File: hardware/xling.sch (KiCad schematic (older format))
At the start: 54 parts, among them J4 USB_OTG, J5 AVR ISP, J6 Battery, Q1 NTR0202PL, Q2 NTR0202PL, Q3 NTA4153N, SW2 BTN, SW3 BTN, SW4 BTN, U1 LT1109CZ-12, U2 ATMEGA328P-AU, U3 DEP_128064I, U4 MCP73831, U5 AP3401_TSOT26, Y1 8MHz

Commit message: patch 0.2.5: New OLED.
There is a huge change in a circuit to replace an OLED and fix multiple
mistakes and improve it a bit.
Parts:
- removed C10: 33uF, Xling Footprints:CP_EIA-6032-20_AVX-F, symbol xling:CP
- removed D3: 1N5818, Xling Footprints:D_DO-41_SOD81_P7.62mm_Horizontal, symbol xling:1N5818
- removed L2: 22uH, Xling Footprints:L_7.3x7.3_H3.5, symbol xling:L_Core_Ferrite
- removed Q2: NTR0202PL, Xling Footprints:SOT-23, symbol xling:NTR2101P
- removed Q3: NTA4153N, Xling Footprints:SC-75_SOT-416, symbol xling:NTA4153N
- removed R1, R10: 100K, Xling Footprints:R_1206_3216Metric, symbol xling:R
- removed R11: 191K, Xling Footprints:R_0805_2012Metric, symbol xling:R
- removed R16: 27K, Xling Footprints:R_0603_1608Metric, symbol xling:R
- removed R2: 910K, Xling Footprints:R_1206_3216Metric, symbol xling:R
- removed U1: LT1109CZ-12, Xling Footprints:TO-92_LT1109CZ, symbol xling:LT1109CZ-12
- removed U3: DEP_128064I, Xling Footprints:XF2M_24151AR100_SMD_1x24_Pitch_0.5mm, symbol xling:DEP_128064I
- added C10: 0.22uF, Xling Footprints:C_0603_1608Metric, symbol xling:C
- added C12, C2, C3, C4: 4.7uF, symbol xling:C
- added C7: 100nF, symbol xling:C
- added L1: 10uH, symbol xling:L
- added R3: 10K, symbol xling:R
- added R6, R7: 510K, Xling Footprints:R_0603_1608Metric, symbol xling:R
- added U1: REX012864L, Xling Footprints:DisplayPin_1x30_P0.7mm, symbol xling:REX012864L
- C1: renamed from C7; footprint Xling Footprints:C_0805_2012Metric -> (none); Model CC0805KRX7R9BB472 -> (none)
- C11: value 2.2uF -> 0.22uF; Model 0603ZD225KAT2A -> (none)
- C13: renamed from C20; footprint Xling Footprints:C_0805_2012Metric -> (none); Model CC0805KRX7R9BB472 -> (none)
- C14: renamed from C19; footprint Xling Footprints:C_0805_2012Metric -> (none); Model CC0805KRX7R9BB472 -> (none)
- C15: renamed from C18; footprint Xling Footprints:C_0805_2012Metric -> (none); Model CC0805KRX7R9BB472 -> (none)
- C16: renamed from C1; footprint Xling Footprints:C_0805_2012Metric -> (none); Model CL21C220JBANNNC -> (none)
- C17: renamed from C6; footprint Xling Footprints:C_1206_3216Metric -> (none); Model CL31B475KAHNNNE -> (none)
- C18: renamed from C2; footprint Xling Footprints:C_1206_3216Metric -> (none); Model CL31B475KAHNNNE -> (none)
- C19: renamed from C5; footprint Xling Footprints:C_1206_3216Metric -> (none); Model CL31B475KAHNNNE -> (none)
- C20: renamed from C3; footprint Xling Footprints:C_1206_3216Metric -> (none); Model CL31B475KAHNNNE -> (none)
- C5: renamed from C15; footprint Xling Footprints:C_0805_2012Metric -> (none); Model CL21C220JBANNNC -> (none)
- C6: renamed from C8; footprint Xling Footprints:C_0805_2012Metric -> (none); Model CL21B104JBCNNNC -> (none)
- C8: renamed from C13; footprint Xling Footprints:C_0805_2012Metric -> (none); Model CL21C220JBANNNC -> (none)
- C9: value 1pF -> 100nF; footprint Xling Footprints:C_0805_2012Metric -> (none); Model CL21C010BBANNNC -> (none)
- D1: renamed from D5; value 1N5818 -> 1N5819; footprint Xling Footprints:D_DO-41_SOD81_P7.62mm_Horizontal -> (none); Model 1N5819 -> 1N5819HW-7-F
- J1: renamed from J5; value AVR ISP -> ISP; footprint Xling Footprints:IDC-Header_2x03_P2.54mm_Vertical -> (none); Model T821106A1S100CEU -> (none)
- J2: renamed from J4; footprint Xling Footprints:USB_Mini-B_Lumberg_2486_01_Horizontal -> (none); Model Molex 67503-1020 -> 105017-0001
- J3: renamed from J6; footprint Xling Footprints:PinHeader_1x02_P2.54mm_Horizontal -> (none); Model DS1022-1*20RDF1-1 -> (none)
- L2: renamed from L1; footprint Xling Footprints:L_1210_3225Metric -> (none); Model NLV10JT2R2 -> NLV32T-2R2J-PF
- R10: renamed from R17; footprint Xling Footprints:R_1206_3216Metric -> (none); Model CRCW1206100KFKTABC -> (none)
- R11: renamed from R6; footprint Xling Footprints:R_1206_3216Metric -> (none); Model CRCW1206100KFKTABC -> (none)
- R13: footprint Xling Footprints:R_1206_3216Metric -> (none); Model CRCW1206100KFKTABC -> (none)
- R14, R15: value 27K -> 510K; Model CRCW060327K0FKTABC -> 0603SAJ0514T5E
- R16: renamed from R3; value 4K3 -> 2.55K; Model 0603SAJ0432T5E -> (none)
- R17: renamed from R12; footprint Xling Footprints:R_0805_2012Metric -> (none); Model CRCW0805110KJNTABC -> (none)
- R18: renamed from R20; footprint Xling Footprints:R_0805_2012Metric -> (none); Model CRCW0805110KJNTABC -> (none)
- R4, R5: value 100K -> 510K; footprint Xling Footprints:R_1206_3216Metric -> Xling Footprints:R_0603_1608Metric; Model CRCW1206100KFKTABC -> 0603SAJ0514T5E
- R8: renamed from R19; footprint Xling Footprints:R_1206_3216Metric -> (none); Model CRCW1206100KFKTABC -> (none)
- R9: renamed from R18; footprint Xling Footprints:R_1206_3216Metric -> (none); Model CRCW1206100KFKTABC -> (none)
- SW1: renamed from SW4; footprint Xling Footprints:SW_SPST_PTS645 -> (none); Model KSC241JLFS -> (none)
- SW2: renamed from SW3; footprint Xling Footprints:SW_SPST_PTS645 -> (none); Model KSC241JLFS -> (none)
- SW3: renamed from SW2; footprint Xling Footprints:SW_SPST_PTS645 -> (none); Model KSC241JLFS -> (none)
- U3: renamed from U4; Model MCP73831T-2AT -> MCP73831T-2ATI/OT
- Y1: footprint Xling Footprints:Crystal_HC49-SD_SMD -> (none); Model LF XTAL003151 -> LFXTAL055663BULK
- renumbered R8 to R1, R7 to R12, R9 to R2, U5 to U4
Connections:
- net OLED_VCC is gone; now on net ISP_RST: C9.1
- net +3V3: now also R5.2, C3.1, C4.1, L1.1, R3.2, R6.2, R7.2, U1.11 (IM1), U1.15 (A0(SA0)), U1.6 (VDD2), U1.9 (VDD1); no longer C6.1, R14.1, R15.1, R5.1, U2.18 (AVCC)
- net BAT_LVL: now also R14.1, U2.19 (ADC6); no longer U2.23 ((PCINT8/ADC0)PC0)
- net GND: now also C5.1, C8.1, R15.1, R4.1, C12.2, C2.2, C3.2, C4.2, C7.2, U1.10 (IM0), U1.12 (IM2), U1.13 (~CS~(CSB)), U1.16 (~WR~(WRB/R/~W~)), U1.17 (~RD~(RDB/E)), U1.29 (VLSS), U1.8 (VSS); no longer C11.2, C5.2, C8.2, R4.2, U2.20 (AREF)
- net ISP_RST: now also R3.1
- net OLED_RES: now also U1.14 (~RES~(RESB))
- net OLED_SCL: now also R1.2, U1.18 (D0(SCL)); no longer R2.2
- net OLED_SDA: now also R2.2, U1.19 (D1(SDA/SI)); no longer R1.2
- net at C20.1, D1.2 (A), J2.1 (VBUS)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: now also R15.2; no longer R4.1
- net at U2.8 ((PCINT7/XTAL2/TOSC2)PB7), Y1.1: now also C8.2; no longer C5.1
- net at U2.7 ((PCINT6/XTAL1/TOSC1)PB6), Y1.2: now also C5.2; no longer C8.1
- net at R10.2, SW3.1: now also R7.1; no longer R14.2
- net at R9.2, SW2.1: now also R6.1; no longer R15.2
- net at R8.2, SW1.1: now also R5.1
- net at C17.1, J3.1 (Pin_1), Q1.3 (D)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: now also R14.2
- net at C11.1: now also U1.4 (C2P)
- new net: C6.1, L1.2, U2.18 (AVCC)
- new net: C7.1, U2.20 (AREF)
- new net: C10.1, U1.2 (C1N)
- new net: R4.2, U1.26 (IREF)
- new net: C12.1, U1.27 (VCOMH)
- new net: C2.1, U1.28 (VPP)
- new net: C10.2, U1.3 (C1P)
- new net: C11.2, U1.5 (C2N)
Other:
- note added: "AVR ISP connector"
- note added: "Controller: SH1106G\nVDD1: 1.65-3.5V\nVDD2: 3.0-4.7V\nMode: I2C\nAddress: 0x3D, but\n LSB denotes a mode, so\n 0x7A - to write,\n 0x7B - to read)"
- note added: "Microcontroller"
- note added: "Power supply"
- note added: "Regulator of the battery charge current (R3):\n\nIreg = 1000V/Rprog, where\nIreg - charge current, in mA\nR3 - resistor value, in kOhm.\n\nR3 = 1000/400 = 2.5kOhm,\nStandard value is 2.55 kOhm (1%),\nIreg ~~ 392mA"
- note added: "Resistor devider R7-R20:\n\nR7 = R20*(Vout/0.6-1) =\n(110*10^3)*(3.3/0.6-1) =\n~~510 kOhm"
- note added: "Set IREF to 12.5uA:\n(V at IREF-VSS)/Iref =\n(6.4V-0)/12.5uA =\n512kΩ\n\nCharge pump output\nvoltage: 6.4V-9.0V"
- note added: "This circuit produces 3.3V and charges a battery when\nconnected to USB.\n\nThis can be done by providing a 5V USB (~~4.6V after a\nvoltage drop on 1N5819) to fill needs of the whole circuit\nvia AP3401 and charge a single-cell 3.7V Li-Ion battery\nusing MCP73831 (MOSFET is closed).\n\nThe circuit can also be powered by the battery only\nchanging its voltage down to 3.3V via AP3401 (MOSFET is ope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"
- note removed: "*\n* Including model files\n*\n*.include NTA4001NT1.LIB\n.include NTA4153N.REV0.LIB\n.include NTR0202PL.REV0.LIB\n*\n* Components of the scheme\n*\nR10 0 1 100k\nR5 2 3 100k\n* R3 - pull-down resistor to prove an output is floating contact when\n* XQ2 is closed\n*R3 4 0 100k\nC9 4 0 1p\nXQ3 2 1 0 nta4153n\nXQ2 4 2 3 ntr0202plt1\nVIN 1 0 pulse (0 3.15 2ms 0ns 0ms 5ms 10ms)\nVDD 3 0 pwl (0 0 0ms 0 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"
- note removed: "22uH, 0.19Ω\nFERROCORE\nDE0703-22"
- note removed: "3.3V-to-12V DC-DC"
- note removed: "3.3V-to-12V Switch"
- note removed: "3.3V-to-12V Switch (ngspice .cir)"
- note removed: "Battery (charge) current regulator\nbased on a resistor R3:\n\nIreg = 1000V/Rprog, where\nIreg - charge current, in mA\nRprog - resistor value (R3), in kOhm.\n\nRprog = 1000/250 = 4kOhm,\nStandard value is 4.3kOhm, Ireg ~~ 232mA"
- note removed: "Controller:\nVDD:\nVCC:\nMode:\nAddress:"
- note removed: "Current Direction (Q1 based, ngspice .cir)"
- note removed: "Current Direction Control Circuit based on a single P-Channel MOSFET\n\n* Including model files\n*.include NTA4001NT1.LIB\n.include NTA4153N.REV0.LIB\n.include NTR0202PL.REV0.LIB\n.include 1N5819.LIB\n\n* Components of the scheme\nR1 0 1 100k\nR2 0 2 12\nC1 0 3 4.7u\nC2 0 2 4.7u\nXQ1 3 1 2 ntr0202plt1\nD1 1 2 D1n5819\nVIN 1 0 pulse (0 4.95 2ms 0ns 0ms 5ms 10ms)\nVDD 3 0 pwl (0 0 0ms 0 0ms 3.2v 20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"
- note removed: "It is recommended to set Iref to 10±2uA:\nR2 = (Vcc-3)/Iref = (12V-3V)/10uA = 900kΩ"
- note removed: "Main microcontroller"
- note removed: "Power required from the inductor:\nPl = (Vout+Vd-Vin)*Iout = (12V+0.5V-3.3V)(45mA) = 414mW\n\nEnergy required by the inductor per cycle must be >=:\nPl/Fosc = 414mW/120kHz = 3.45 uJ\n\nPicking an inductor value of 22μH with 0.19R DCR\nresults in a peak switch current of:\nIpeak = (3.3V/(0.8R+0.19R))*(1-e^((-1.0*4.2us)/(22uH))) = 579mA\n\nOnce Ipeak is known, energy in the inductor at the end\nof 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"
- note removed: "Power supply and battery charger"
- note removed: "Resistor devider:\nR6 = R7*(Vout/0.6-1) =\n(110*10^3)*(3.3/0.6-1) ~~ 510kOhm"
- note removed: "SSD1309ZC\n2.8-3.3V\n12V\nI2C\n0x7A"
- note removed: "The main idea of a scheme is to produce 3.3V and charge\na battery while sharing load between a USB power and a power\nobtained from the battery."
- note removed: "This can be achieved by providing a 5V USB (~~4.6V after\nvoltage drop on D5) to fill needs of the whole circuit via\nAP3401 and charge a 3.7V Li-Ion or Li-Polymer battery\nusing MCP73831 battery controller, on one hand (Q1 will be\nclosed in this case). On the other, the whole scheme can work \nautonomously using the battery and changing its voltage\ndown to 3.3V via AP3401 (Q1 will be open)."
- note removed: "This switch is based on N-Channel and\nP-Channel MOSFETs to power on and off\nOLED display. This is necessary to use\na logic level 3.3V to switch 12V and\nleave Vcc contact floating when\nNTR0202PL is closed."
- note removed: "max.\n45mA"
- note removed: "tantalum\nlow ESR 0.1Ω\nAVX TPSC336K016R0150"
- moved on the sheet: C1, C13, C14, C15, C16, C17, C18, C19, C20, C5, C6, C8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

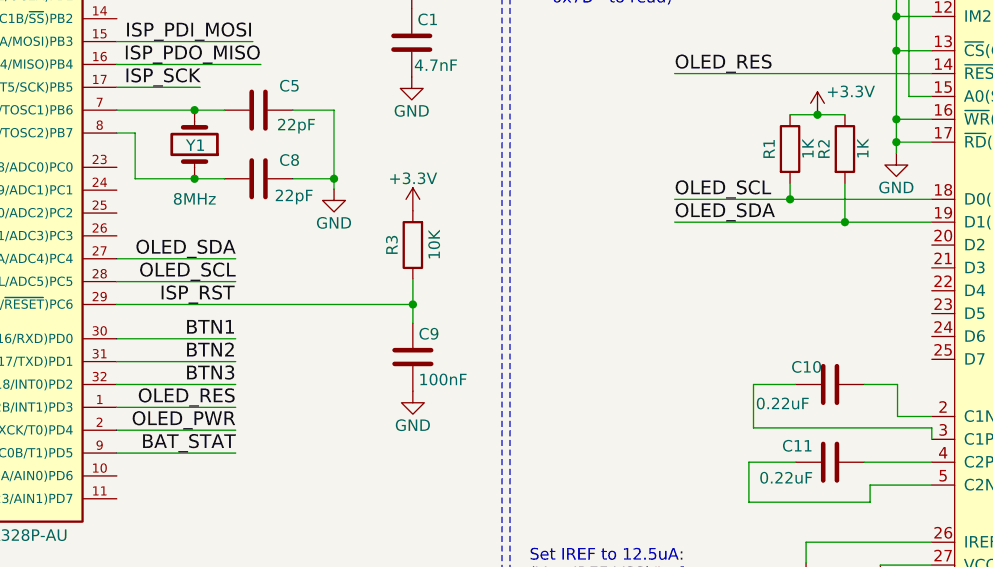
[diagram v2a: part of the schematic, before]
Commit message: patch 0.2.6: Update and add missing footprints.
ticket: N/A

There new models/parts found for micro switches and a connector for AVR
in-circuit system programmer.
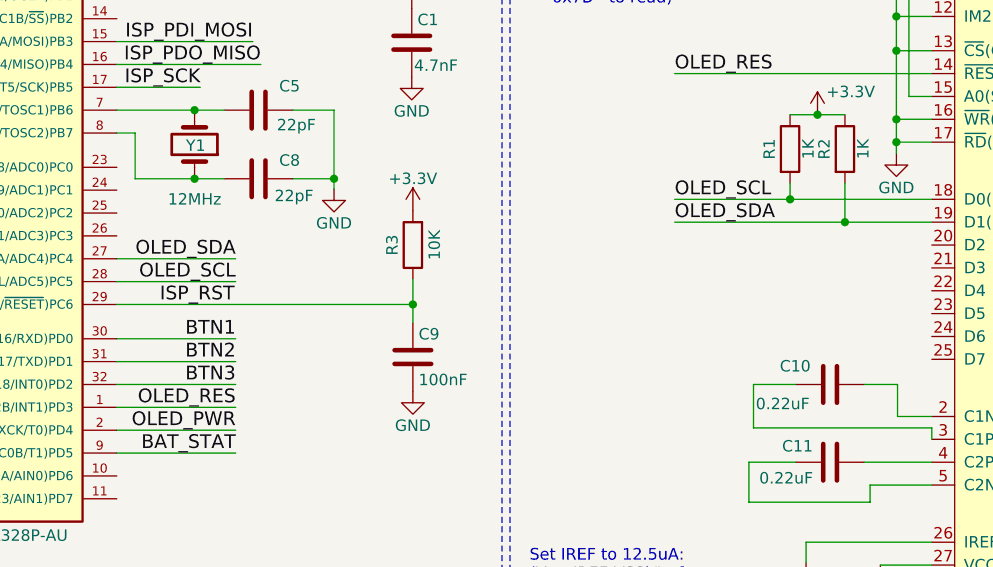
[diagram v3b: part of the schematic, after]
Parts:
- C1, C13, C14, C15: footprint (none) -> Xling Footprints:C_0603_1608Metric; Model (none) -> CL10B472KB8NNNC
- C10, C11: Model (none) -> CL10B224KO8NNNC
- C12, C17, C18, C19, C2, C20, C3, C4: footprint (none) -> Xling Footprints:C_0603_1608Metric; Model (none) -> CL10A475KQ8NNNC
- C16, C5, C8: footprint (none) -> Xling Footprints:C_0603_1608Metric; Model (none) -> CL10C220JB8NNNC
- C6, C7, C9: footprint (none) -> Xling Footprints:C_0603_1608Metric; Model (none) -> CL10B104KO8NNNC
- D1: footprint (none) -> Xling Footprints:D_SOD-123
- J1: footprint (none) -> Xling Footprints:Molex_Pico-Lock_504050-0691_1x06-1MP_P1.50mm_Horizontal; Model (none) -> 504050-0691
- J2: footprint (none) -> Xling Footprints:USB_Micro-B_Molex-105017-0001
- L1, L2: footprint (none) -> Xling Footprints:L_1210_3225Metric
- R10, R11, R13, R8, R9: footprint (none) -> Xling Footprints:R_0603_1608Metric; Model (none) -> 0603SAJ0104T5E
- R16: Model (none) -> 0603SAF2551T5E
- R17, R18: footprint (none) -> Xling Footprints:R_0603_1608Metric; Model (none) -> 0603SAF1103T5E
- R3: footprint (none) -> Xling Footprints:R_0603_1608Metric; Model (none) -> 0603SAJ0103T5E
- SW1, SW2, SW3: footprint (none) -> Xling Footprints:SW_Tact_4.5x4.5mm_TVCM09BB_Low_Profile; Model (none) -> TVCM09BB
- Y1: value 8MHz -> 12MHz; footprint (none) -> Xling Footprints:Crystal_SMD_CFPX-104-4Pin_5x3.2mm; Model LFXTAL055663BULK -> LFXTAL032878BULK

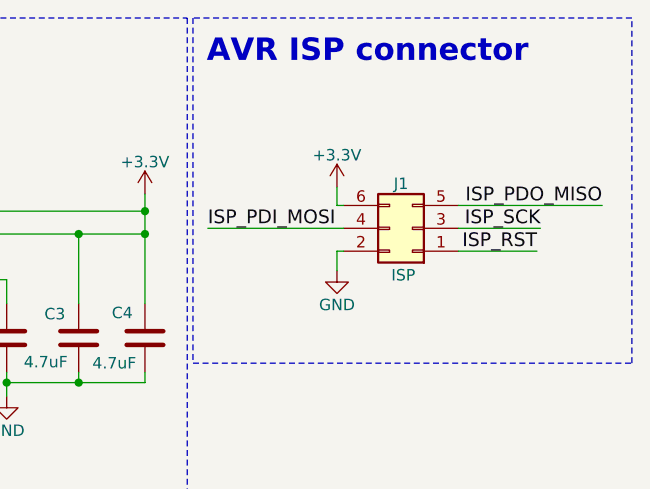
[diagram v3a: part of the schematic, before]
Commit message: patch 0.2.7: PCB adjustments.
ticket: N/A

There are some modifications to make a new version of the PCB ready for
manufacturing.
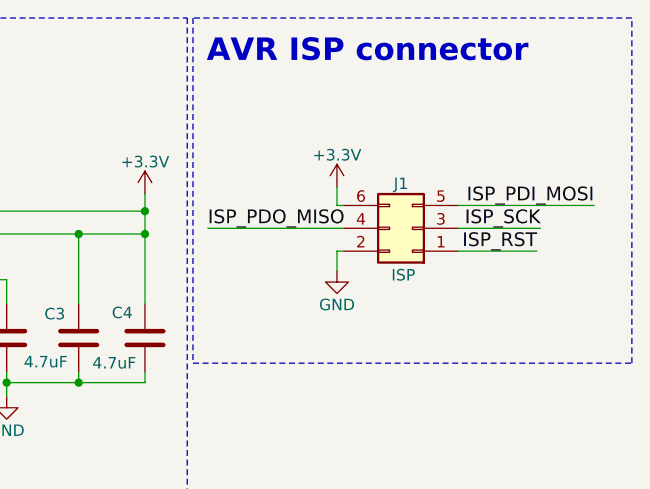
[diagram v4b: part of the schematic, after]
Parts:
- J3: footprint (none) -> Xling Footprints:PinHeader_1x02_P2.54mm_Vertical
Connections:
- net ISP_PDI_MOSI: now also J1.5 (Pin_5); no longer J1.4 (Pin_4)
- net ISP_PDO_MISO: now also J1.4 (Pin_4); no longer J1.5 (Pin_5)
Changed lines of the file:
@@
 Title "Xling Circuit"
 Date "2019-02-13"
-Rev "0.2.6"
+Rev "0.2.7"
 Comp ""
 Comment1 ""
@@
 Text Label 3600 1760 2    60   ~ 0
 ISP_PDO_MISO
+Text Label 11025 1325 2    60   ~ 0
+ISP_PDI_MOSI
 Text Label 9335 1425 0    60   ~ 0
-ISP_PDI_MOSI
-Text Label 11060 1325 2    60   ~ 0
 ISP_PDO_MISO
 $Comp
@@
 F 0 "J3" H 3145 7240 50  0000 C CNN
 F 1 "Battery" H 3115 6890 50  0000 C CNN
-F 2 "" H 3145 7120 50  0001 C CNN
+F 2 "Xling Footprints:PinHeader_1x02_P2.54mm_Vertical" H 3145 7120 50  0001 C CNN
 F 3 "" H 3145 7120 50  0001 C CNN
 	1    3145 7120
@@
 	9930 1425 9335 1425
 Wire Wire Line
-	10430 1325 11060 1325
-Wire Wire Line
 	10430 1425 10790 1425
 Wire Wire Line
@@
 Wire Notes Line
 	11190 2015 11190 505
+Wire Wire Line
+	10430 1325 11025 1325
 $EndSCHEMATC

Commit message: patch 0.2.9: New battery SMD footprint.
ticket: N/A
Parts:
- J3: footprint Xling Footprints:PinHeader_1x02_P2.54mm_Vertical -> Xling Footprints:Battery_SMD_pads_1x02_HandSoldering
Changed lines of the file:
@@
 Title "Xling Circuit"
 Date "2019-02-13"
-Rev "0.2.8"
+Rev "0.2.9"
 Comp ""
 Comment1 ""
@@
 F 0 "J3" H 3145 7240 50  0000 C CNN
 F 1 "Battery" H 3115 6890 50  0000 C CNN
-F 2 "Xling Footprints:PinHeader_1x02_P2.54mm_Vertical" H 3145 7120 50  0001 C CNN
+F 2 "Xling Footprints:Battery_SMD_pads_1x02_HandSoldering" H 3145 7120 50  0001 C CNN
 F 3 "" H 3145 7120 50  0001 C CNN
 	1    3145 7120

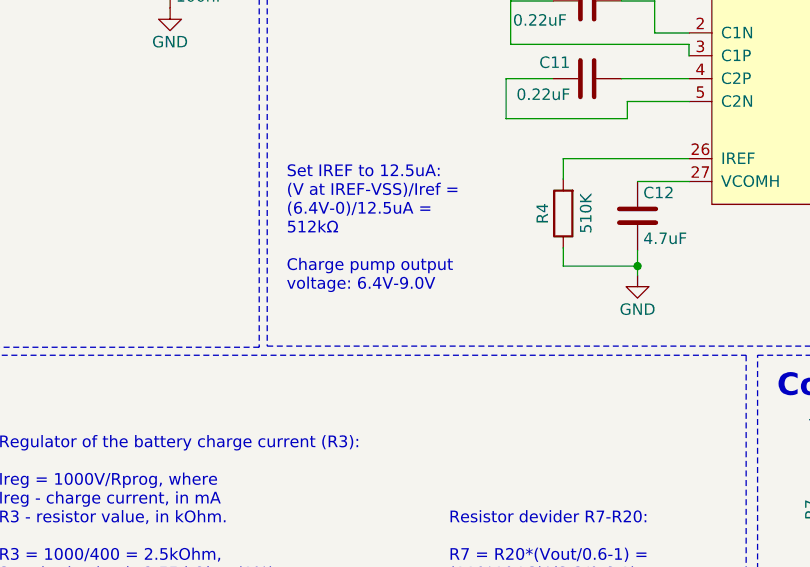
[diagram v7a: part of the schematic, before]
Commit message: patch 0.2.11: Little adjustments to schematic.
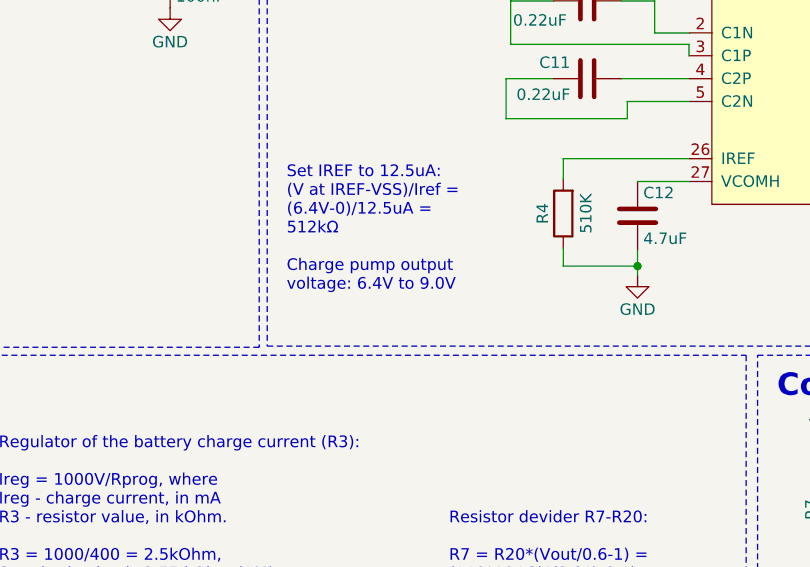
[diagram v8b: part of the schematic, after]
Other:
- note added: "Set IREF to 12.5uA:\n(V at IREF-VSS)/Iref =\n(6.4V-0)/12.5uA =\n512kΩ\n\nCharge pump output\nvoltage: 6.4V to 9.0V"
- note removed: "Set IREF to 12.5uA:\n(V at IREF-VSS)/Iref =\n(6.4V-0)/12.5uA =\n512kΩ\n\nCharge pump output\nvoltage: 6.4V-9.0V"
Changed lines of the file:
@@
 encoding utf-8
 Sheet 1 1
-Title "Xling Circuit"
-Date "2019-02-13"
-Rev "0.2.10"
+Title "Xling Tamagotchi-like Game"
+Date "2019-04-04"
+Rev "0.2.11"
 Comp "Designed by Dmitry Salychev"
 Comment1 ""
 Comment2 ""
-Comment3 "It is designed as a hobby game within the MCUSim project."
-Comment4 "Tamagotchi-like device with OLED and Li-Ion battery."
+Comment3 "It is designed as a hobby toy within the MCUSim project."
+Comment4 "A tamagotchi-like game with an OLED display and Li-Ion battery."
 $EndDescr
 $Comp
@@
 $EndComp
 Text Notes 4775 4435 0    51   ~ 0
-Set IREF to 12.5uA:\n(V at IREF-VSS)/Iref =\n(6.4V-0)/12.5uA =\n512kΩ\n\nCharge pump output\nvoltage: 6.4V-9.0V
+Set IREF to 12.5uA:\n(V at IREF-VSS)/Iref =\n(6.4V-0)/12.5uA =\n512kΩ\n\nCharge pump output\nvoltage: 6.4V to 9.0V
 Text Notes 5485 5785 0    51   ~ 0
 Resistor devider R7-R20:\n\nR7 = R20*(Vout/0.6-1) =\n(110*10^3)*(3.3/0.6-1) =\n~~510 kOhm
